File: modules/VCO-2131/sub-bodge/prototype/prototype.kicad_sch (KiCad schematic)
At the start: 4 parts, among them J1 Conn_01x09, U1 74HCS74

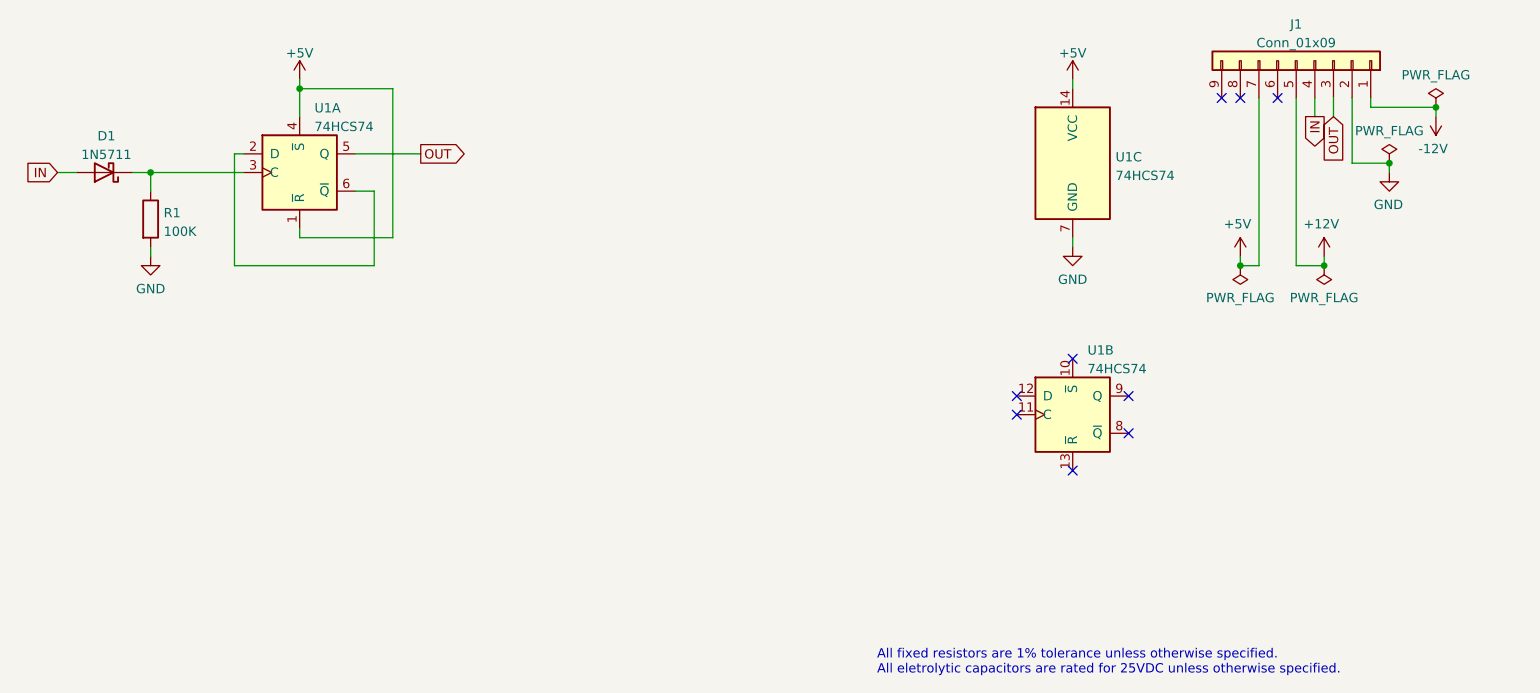
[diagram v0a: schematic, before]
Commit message: VCO sub fix - PCB with SOIC
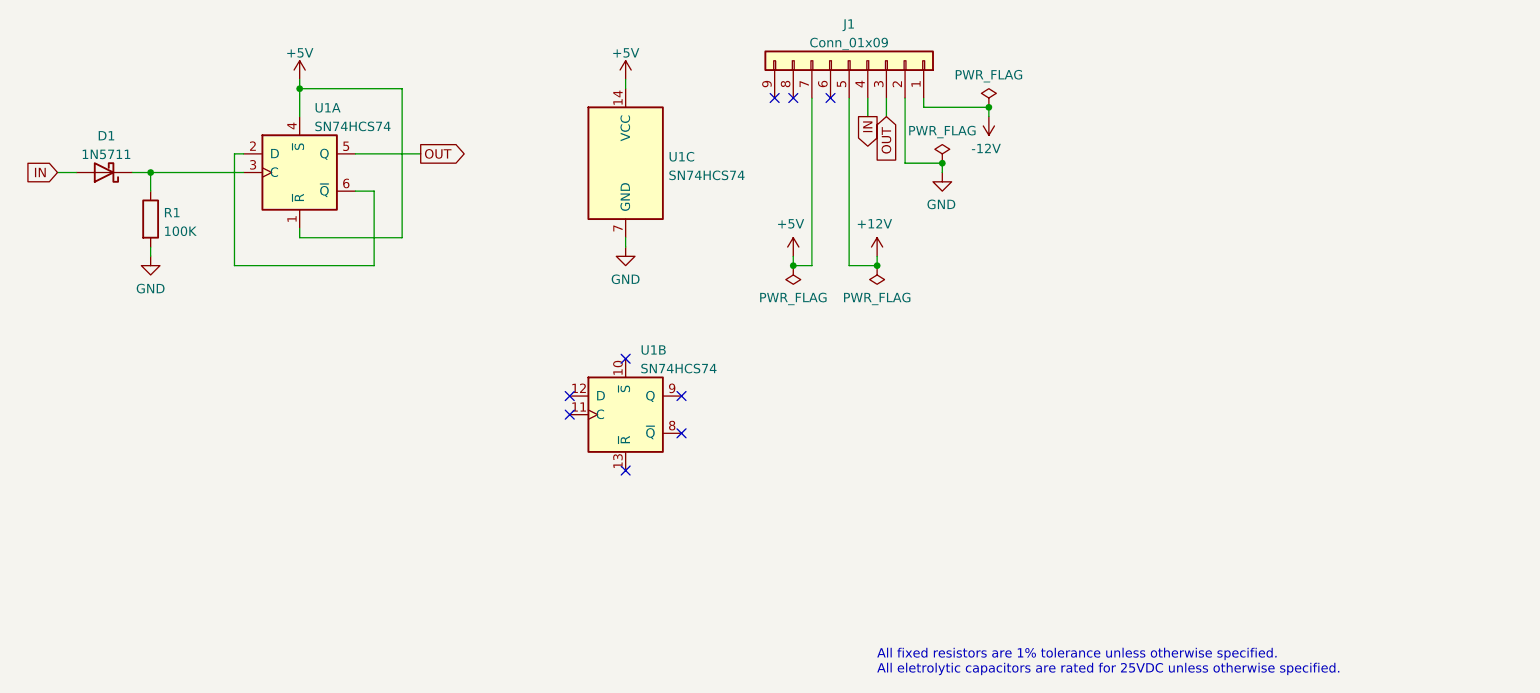
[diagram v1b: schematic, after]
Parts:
- U1: value 74HCS74 -> SN74HCS74; symbol 74xx:74HC74 -> -lmp-IC-misc:SN74HCS74; Distributor (none) -> Mouser; DistributorPartLink (none) -> https://www.mouser.ca/ProductDetail/Texas-Instruments/SN74H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; DistributorPartNum (none) -> 595-SN74HCS74DR; Manufacturer (none) -> Texas Instruments; ManufacturerPartNum (none) -> SN74HCS74DR
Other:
- moved on the sheet: J1, U1B, U1C

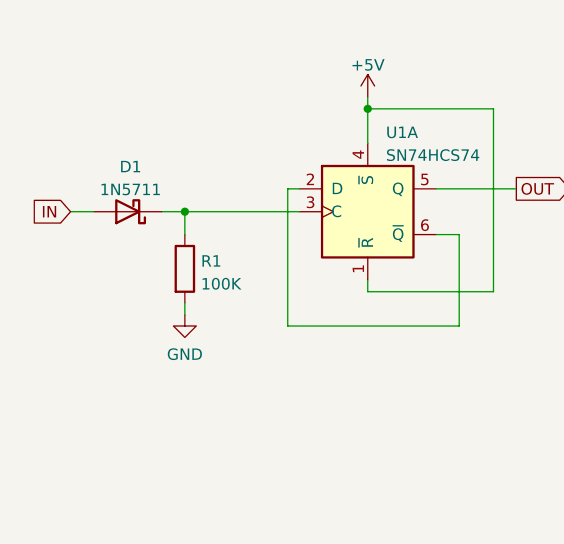
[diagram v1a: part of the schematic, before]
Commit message: VCO sub fix - try again
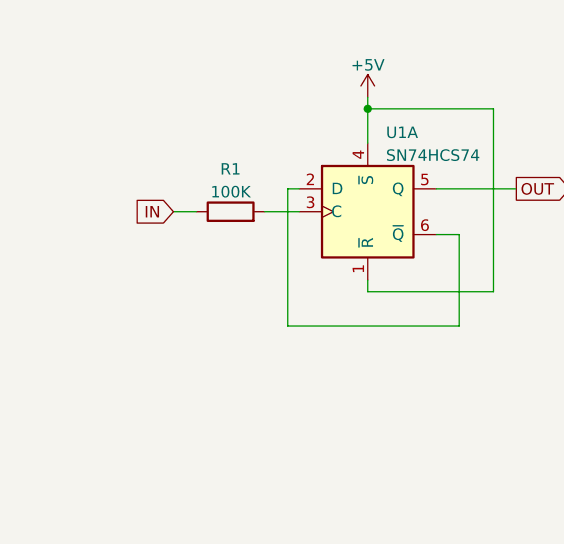
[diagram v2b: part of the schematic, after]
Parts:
- removed D1: 1N5711, Diode_THT:D_DO-35_SOD27_P7.62mm_Horizontal, symbol -lmp-diode:1N5711
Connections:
- net GND: no longer R1.2
- net IN: now also R1.1
- net at U1.3 (C): now also R1.2; no longer R1.1
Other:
- moved on the sheet: R1
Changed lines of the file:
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@@
     (comment 2 "Circuit design for my custom Eurorack breadboard prototyping module")
-  )
-  (junction (at 78.74 87.63) (diameter 0) (color 0 0 0 0)
   )
   (junction (at 186.69 86.36) (diameter 0) (color 0 0 0 0)
@@
   (no_connect (at 163.83 77.47))
   (no_connect (at 166.37 77.47))
-  (wire (pts (xy 66.04 87.63) (xy 68.58 87.63))
+  (wire (pts (xy 77.47 87.63) (xy 80.01 87.63))
     (stroke (width 0) (type default) (color 0 0 0 0))
   )
@@
     (stroke (width 0) (type default) (color 0 0 0 0))
   )
-  (wire (pts (xy 78.74 87.63) (xy 91.44 87.63))
-    (stroke (width 0) (type default) (color 0 0 0 0))
-  )
-  (wire (pts (xy 78.74 97.79) (xy 78.74 99.06))
-    (stroke (width 0) (type default) (color 0 0 0 0))
-  )
   (wire (pts (xy 113.03 96.52) (xy 113.03 76.2))
     (stroke (width 0) (type default) (color 0 0 0 0))
@@
     (stroke (width 0) (type default) (color 0 0 0 0))
   )
-  (wire (pts (xy 76.2 87.63) (xy 78.74 87.63))
+  (wire (pts (xy 87.63 87.63) (xy 91.44 87.63))
     (stroke (width 0) (type default) (color 0 0 0 0))
   )
@@
   )
   (wire (pts (xy 173.99 77.47) (xy 173.99 100.33))
-    (stroke (width 0) (type default) (color 0 0 0 0))
-  )
-  (wire (pts (xy 78.74 87.63) (xy 78.74 90.17))
     (stroke (width 0) (type default) (color 0 0 0 0))
   )
@@
     (effects (font (size 1.27 1.27)) (justify left bottom))
   )
-  (global_label "IN" (shape input) (at 66.04 87.63 180) (fields_autoplaced)
+  (global_label "IN" (shape input) (at 77.47 87.63 180) (fields_autoplaced)
     (effects (font (size 1.27 1.27)) (justify right))
-    (property "Intersheet References" "${INTERSHEET_REFS}" (id 0) (at 61.7806 87.5506 0)
+    (property "Intersheet References" "${INTERSHEET_REFS}" (id 0) (at 73.2106 87.5506 0)
       (effects (font (size 1.27 1.27)) (justify right) hide)
     )
@@
     (pin "1")
   )
-  (symbol (lib_id "-lmp:R") (at 78.74 93.98 0) (unit 1)
-    (in_bom yes) (on_board yes) (fields_autoplaced)
-    (property "Reference" "R1" (id 0) (at 80.518 93.1453 0)
-      (effects (font (size 1.27 1.27)) (justify left))
-    )
-    (property "Value" "100K" (id 1) (at 80.518 95.6822 0)
-      (effects (font (size 1.27 1.27)) (justify left))
-    )
-    (property "Footprint" "-lmp-misc:R_Axial_DIN0207_L6.3mm_D2.5mm_P7.62mm_Horizontal" (id 2) (at 76.962 93.98 90)
-      (effects (font (size 1.27 1.27)) hide)
-    )
-    (property "Datasheet" "https://www.mouser.ca/datasheet/2/447/Yageo_LR_MFR_1-1714151.pdf" (id 3) (at 78.74 93.98 0)
-      (effects (font (size 1.27 1.27)) hide)
-    )
-    (property "Value2" "1%, 1/6 W" (id 4) (at 83.058 93.98 90)
-      (effects (font (size 1.27 1.27)) hide)
-    )
-    (property "Manufacturer" "YAGEO" (id 5) (at 78.74 93.98 0)
-      (effects (font (size 1.27 1.27)) hide)
-    )
-    (property "ManufacturerPartNum" "MFR-12*" (id 6) (at 78.74 93.98 0)
-      (effects (font (size 1.27 1.27)) hide)
-    )
-    (property "Distributor" "Mouser" (id 7) (at 78.74 93.98 0)
-      (effects (font (size 1.27 1.27)) hide)
-    )
-    (property "DistributorPartNum" "603-MFR-12*" (id 8) (at 78.74 93.98 0)
-      (effects (font (size 1.27 1.27)) hide)
-    )
-    (property "DistributorPartLink" "https://www.mouser.ca/c/passive-components/resistors/film-resistors/metal-film-resistors-through-hole/?m=YAGEO&power%20rating=166%20mW%20%281%2F6%20W%29&tolerance=1%20%25&instock=y" (id 9) (at 78.74 93.98 0)
+  (symbol (lib_id "-lmp:R") (at 83.82 87.63 90) (unit 1)
+    (in_bom yes) (on_board yes) (fields_autoplaced)
+    (property "Reference" "R1" (id 0) (at 83.82 82.9142 90))
+    (property "Value" "100K" (id 1) (at 83.82 85.4511 90))
+    (property "Footprint" "-lmp-misc:R_Axial_DIN0207_L6.3mm_D2.5mm_P7.62mm_Horizontal" (id 2) (at 83.82 89.408 90)
+      (effects (font (size 1.27 1.27)) hide)
+    )
+    (property "Datasheet" "https://www.mouser.ca/datasheet/2/447/Yageo_LR_MFR_1-1714151.pdf" (id 3) (at 83.82 87.63 0)
+      (effects (font (size 1.27 1.27)) hide)
+    )
+    (property "Value2" "1%, 1/6 W" (id 4) (at 83.82 83.312 90)
+      (effects (font (size 1.27 1.27)) hide)
+    )
+    (property "Manufacturer" "YAGEO" (id 5) (at 83.82 87.63 0)
+      (effects (font (size 1.27 1.27)) hide)
+    )
+    (property "ManufacturerPartNum" "MFR-12*" (id 6) (at 83.82 87.63 0)
+      (effects (font (size 1.27 1.27)) hide)
+    )
+    (property "Distributor" "Mouser" (id 7) (at 83.82 87.63 0)
+      (effects (font (size 1.27 1.27)) hide)
+    )
+    (property "DistributorPartNum" "603-MFR-12*" (id 8) (at 83.82 87.63 0)
+      (effects (font (size 1.27 1.27)) hide)
+    )
+    (property "DistributorPartLink" "https://www.mouser.ca/c/passive-components/resistors/film-resistors/metal-film-resistors-through-hole/?m=YAGEO&power%20rating=166%20mW%20%281%2F6%20W%29&tolerance=1%20%25&instock=y" (id 9) (at 83.82 87.63 0)
       (effects (font (size 1.27 1.27)) hide)
     )
     (pin "1")
     (pin "2")
-  )
-  (symbol (lib_id "-lmp-power:GND") (at 78.74 99.06 0) (unit 1)
-    (in_bom yes) (on_board yes) (fields_autoplaced)
-    (property "Reference" "#PWR01" (id 0) (at 78.74 105.41 0)
-      (effects (font (size 1.27 1.27)) hide)
-    )
-    (property "Value" "GND" (id 1) (at 78.74 103.5034 0))
-    (property "Footprint" "" (id 2) (at 78.74 99.06 0)
-      (effects (font (size 1.27 1.27)) hide)
-    )
-    (property "Datasheet" "" (id 3) (at 78.74 99.06 0)
-      (effects (font (size 1.27 1.27)) hide)
-    )
-    (pin "1")
   )
   (symbol (lib_id "-lmp-IC-misc:SN74HCS74") (at 143.51 86.36 0) (unit 3)
@@
     (pin "7")
   )
-  (symbol (lib_id "-lmp-diode:1N5711") (at 72.39 87.63 180) (unit 1)
-    (in_bom yes) (on_board yes) (fields_autoplaced)
-    (property "Reference" "D1" (id 0) (at 72.7075 82.6602 0))
-    (property "Value" "1N5711" (id 1) (at 72.7075 85.1971 0))
-    (property "Footprint" "Diode_THT:D_DO-35_SOD27_P7.62mm_Horizontal" (id 2) (at 72.39 87.63 0)
-      (effects (font (size 1.27 1.27)) hide)
-    )
-    (property "Datasheet" "https://www.mouser.ca/datasheet/2/389/cd00000759-1795802.pdf" (id 3) (at 72.39 87.63 0)
-      (effects (font (size 1.27 1.27)) hide)
-    )
-    (property "Manufacturer" "STMicroelectronics" (id 4) (at 72.39 87.63 0)
-      (effects (font (size 1.27 1.27)) hide)
-    )
-    (property "ManufacturerPartNum" "1N5711" (id 5) (at 72.39 87.63 0)
-      (effects (font (size 1.27 1.27)) hide)
-    )
-    (property "Distributor" "Mouser" (id 6) (at 72.39 87.63 0)
-      (effects (font (size 1.27 1.27)) hide)
-    )
-    (property "DistributorPartNum" "511-1N5711" (id 7) (at 72.39 87.63 0)
-      (effects (font (size 1.27 1.27)) hide)
-    )
-    (property "DistributorPartLink" "https://www.mouser.ca/ProductDetail/STMicroelectronics/1N5711?qs=FITO%2F%2FQgYDnH7pJ7rS2FRA%3D%3D" (id 8) (at 72.39 87.63 0)
-      (effects (font (size 1.27 1.27)) hide)
-    )
-    (pin "1")
-    (pin "2")
-  )
   (sheet_instances
     (path "/" (page "1"))
@@
       (reference "#FLG04") (unit 1) (value "PWR_FLAG") (footprint "")
     )
-    (path "/79458120-e381-43c5-a1a0-df3191f1cc6c"
-      (reference "#PWR01") (unit 1) (value "GND") (footprint "")
-    )
     (path "/6bb3bcf0-5a26-4a16-93d2-d6cae2b5ffdf"
       (reference "#PWR02") (unit 1) (value "+5V") (footprint "")
@@
       (reference "#PWR08") (unit 1) (value "-12V") (footprint "")
     )
-    (path "/e14293fa-70c1-4ed6-90c7-4b2202c47ac8"
-      (reference "D1") (unit 1) (value "1N5711") (footprint "Diode_THT:D_DO-35_SOD27_P7.62mm_Horizontal")
-    )
     (path "/00000000-0000-0000-0000-0000615e2370"
